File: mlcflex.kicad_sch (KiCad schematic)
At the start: 2 parts, among them J1 503398-1892

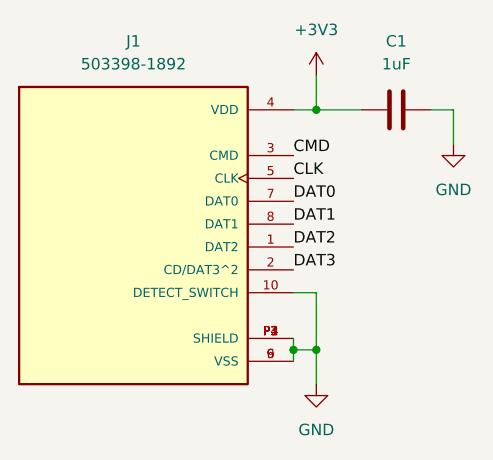
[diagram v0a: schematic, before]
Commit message: Use a 22uF 0805 instead
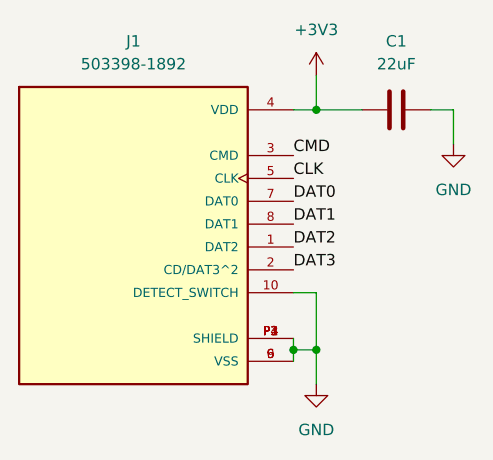
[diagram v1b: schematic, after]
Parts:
- C1: value 1uF -> 22uF; footprint Capacitor_SMD:C_0402_1005Metric -> Capacitor_SMD:C_0805_2012Metric
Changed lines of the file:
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@@
 (kicad_sch
-	(version 20231120)
+	(version 20250114)
 	(generator "eeschema")
-	(generator_version "8.0")
+	(generator_version "9.0")
 	(paper "A4")
 	(junction
@@
 	(label "DAT2"
 		(at 111.76 92.71 0)
-		(fields_autoplaced yes)
 		(effects
 			(font
@@
 	(label "DAT3"
 		(at 111.76 95.25 0)
-		(fields_autoplaced yes)
 		(effects
 			(font
@@
 	(label "DAT0"
 		(at 111.76 87.63 0)
-		(fields_autoplaced yes)
 		(effects
 			(font
@@
 	(label "DAT1"
 		(at 111.76 90.17 0)
-		(fields_autoplaced yes)
 		(effects
 			(font
@@
 	(label "CLK"
 		(at 111.76 85.09 0)
-		(fields_autoplaced yes)
 		(effects
 			(font
@@
 	(label "CMD"
 		(at 111.76 82.55 0)
-		(fields_autoplaced yes)
 		(effects
 			(font
@@
 			)
 		)
-		(property "Value" "1uF"
+		(property "Value" "22uF"
 			(at 123.19 72.39 90)
 			(effects
@@
 			)
 		)
-		(property "Footprint" "Capacitor_SMD:C_0402_1005Metric"
+		(property "Footprint" "Capacitor_SMD:C_0805_2012Metric"
 			(at 127 76.5048 0)
 			(effects
@@
 		)
 	)
+	(embedded_fonts no)
 )
